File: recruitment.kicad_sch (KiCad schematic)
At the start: 18 parts

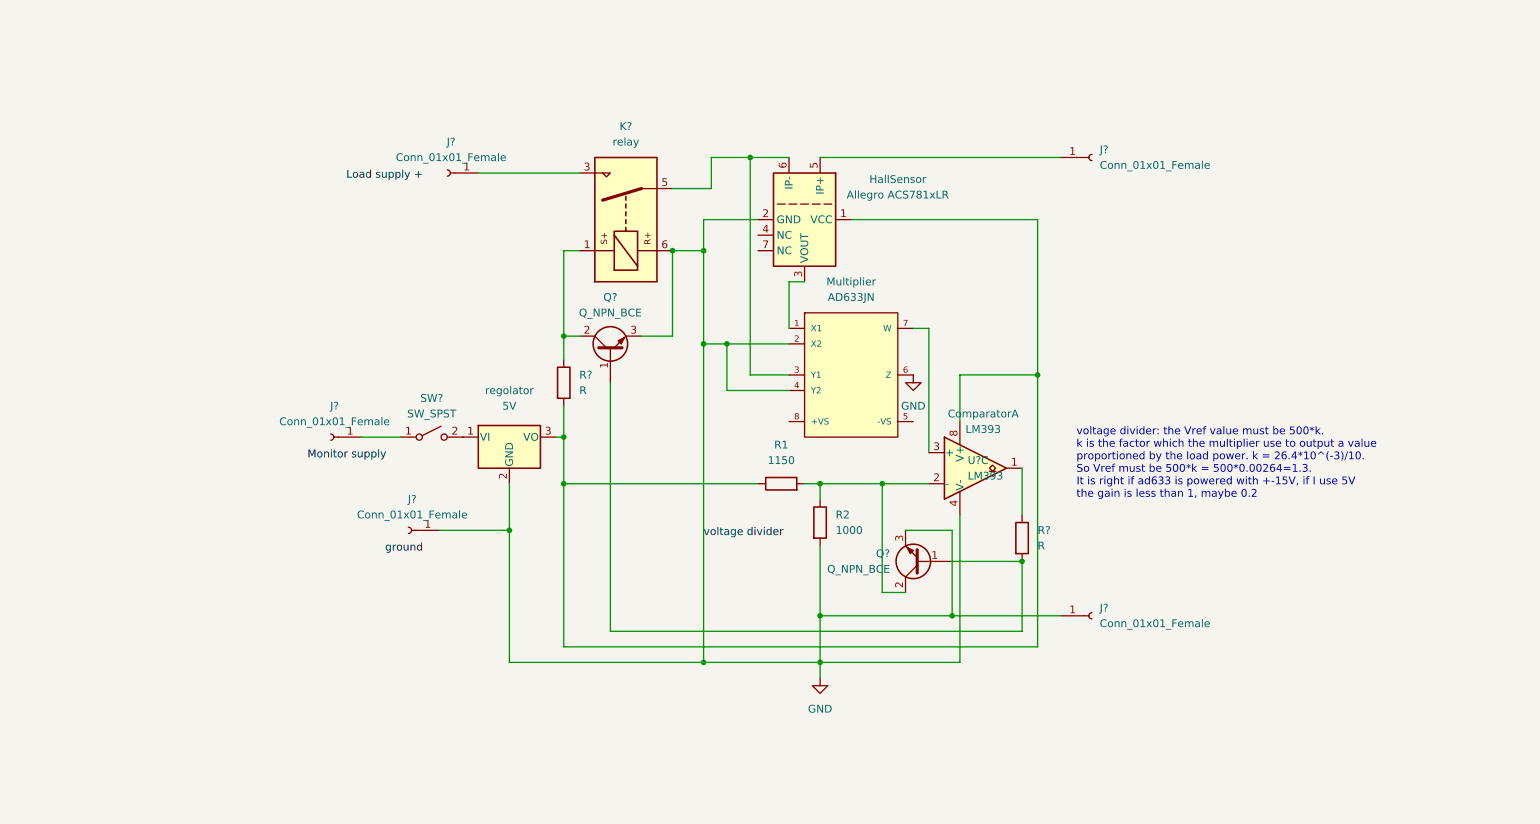
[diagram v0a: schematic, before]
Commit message: TODO: ad633 footprint
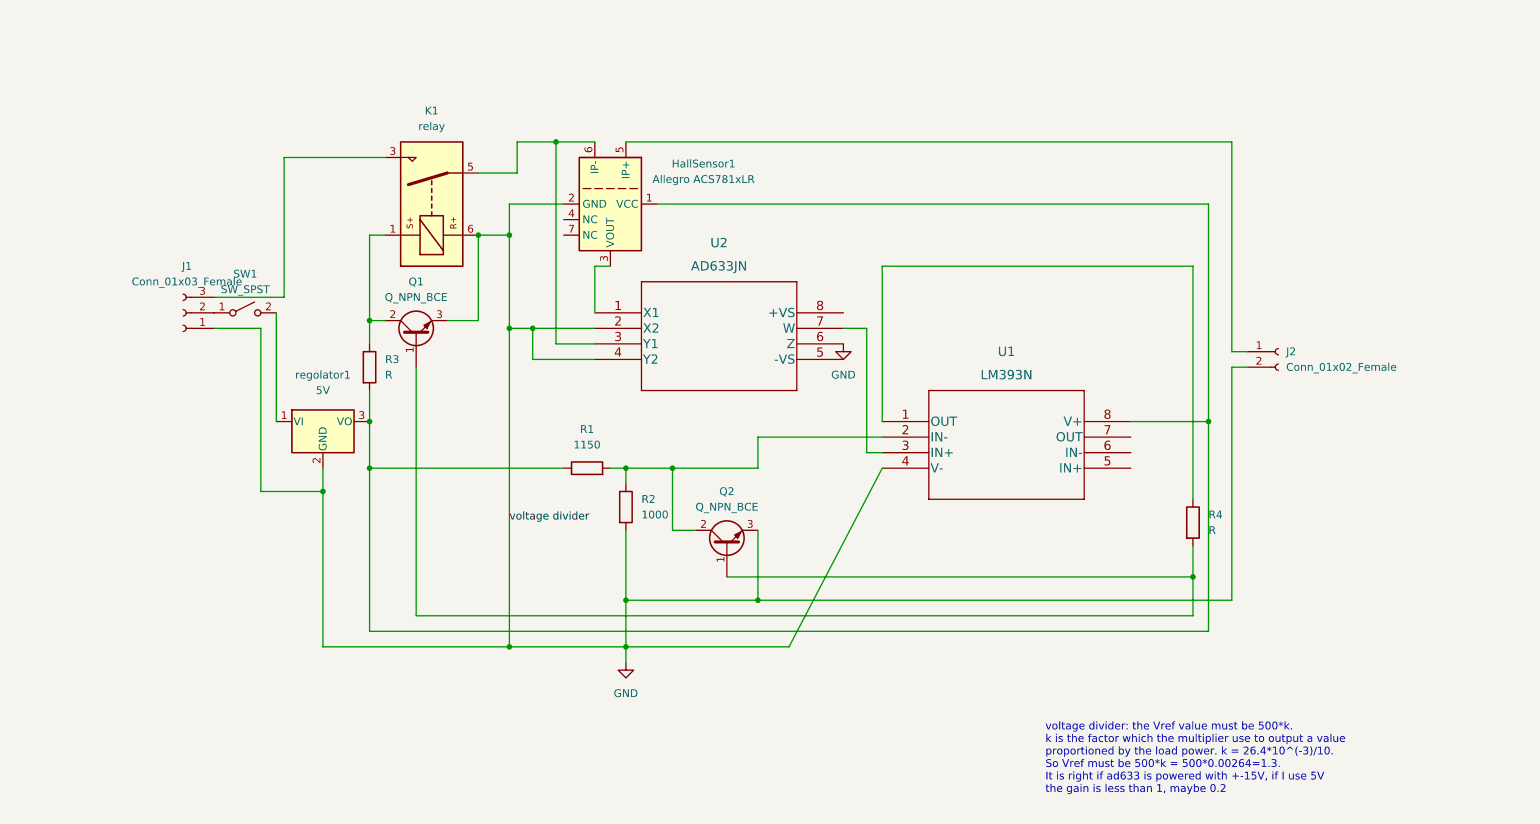
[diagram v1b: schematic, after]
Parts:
- removed Comparator, U?: LM393, symbol Comparator:LM393
- removed J? (x5): Conn_01x01_Female, symbol Connector:Conn_01x01_Female
- removed Multiplier: AD633JN, Analog_Devices-AD633JN-*, symbol eec:AD633JN
- added J1: Conn_01x03_Female, Connector_PinHeader_2.00mm:PinHeader_1x03_P2.00mm_Vertical, symbol Connector:Conn_01x03_Female
- added J2: Conn_01x02_Female, Connector_PinHeader_2.00mm:PinHeader_1x04_P2.00mm_Vertical, symbol Connector:Conn_01x02_Female
- added U1: LM393N, LM393:LM393N, symbol 2023-03-11_20-24-00:LM393N
- added U2: AD633JN, symbol 2023-03-11_21-32-38:AD633JN
- Q1, Q2: renamed from Q?; footprint (none) -> Package_TO_SOT_THT:TO-92_HandSolder
- R1, R2: footprint (none) -> Resistor_SMD:R_2816_7142Metric
- R3, R4: renamed from R?; footprint (none) -> Resistor_SMD:R_2816_7142Metric
- SW1: renamed from SW?; footprint (none) -> Button_Switch_SMD:SW_DIP_SPSTx01_Slide_6.7x4.1mm_W6.73mm_P2.54mm_LowProfile_JPin
- gave numbers to parts that had none: 1
- renumbered HallSensor to HallSensor1, regolator to regolator1
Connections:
- net GND: now also J1.1 (Pin_1), J2.2 (Pin_2), U1.4 (V-), U2.2 (X2), U2.4 (Y2), U2.6 (Z)
- net at Q2.2 (C), R1.2, R2.1: now also U1.2 (IN-)
- net at HallSensor1.1 (VCC), R1.1, R3.2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: now also U1.8 (V+)
- net at HallSensor1.3 (VOUT): now also U2.1 (X1)
- net at HallSensor1.5 (IP+): now also J2.1 (Pin_1)
- net at HallSensor1.6 (IP-), K1.5: now also U2.3 (Y1)
- net at R4.1: now also U1.1 (OUT)
- net at SW1.1 (A): now also J1.2 (Pin_2)
- net at K1.3: now also J1.3 (Pin_3)
- new net: U1.3 (IN+), U2.7 (W)
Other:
- moved on the sheet: HallSensor1, K1, Q1, Q2, R1, R2, R3, R4, SW1, regolator1

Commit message: footprints/autorouting done, TODO: understand transistor and optimize pcb shape
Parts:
- J2: footprint Connector_PinHeader_2.00mm:PinHeader_1x04_P2.00mm_Vertical -> Connector_PinHeader_2.00mm:PinHeader_1x02_P2.00mm_Vertical
- U2: footprint (none) -> LM393:LM393N
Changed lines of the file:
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@@
       (effects (font (size 1.524 1.524)))
     )
-    (property "Footprint" "" (id 2) (at 143.51 73.914 0)
+    (property "Footprint" "LM393:LM393N" (id 2) (at 143.51 73.914 0)
       (effects (font (size 1.524 1.524)) hide)
     )
@@
       (effects (font (size 1.27 1.27)) (justify left))
     )
-    (property "Footprint" "Connector_PinHeader_2.00mm:PinHeader_1x04_P2.00mm_Vertical" (id 2) (at 234.95 86.36 0)
+    (property "Footprint" "Connector_PinHeader_2.00mm:PinHeader_1x02_P2.00mm_Vertical" (id 2) (at 234.95 86.36 0)
       (effects (font (size 1.27 1.27)) hide)
     )
@@
     )
     (path "/9ef2c0bd-0176-4f0e-b213-c48663ceb734"
-      (reference "J2") (unit 1) (value "Conn_01x02_Female") (footprint "Connector_PinHeader_2.00mm:PinHeader_1x04_P2.00mm_Vertical")
+      (reference "J2") (unit 1) (value "Conn_01x02_Female") (footprint "Connector_PinHeader_2.00mm:PinHeader_1x02_P2.00mm_Vertical")
     )
     (path "/b4450c83-6da6-4393-a892-92bf8cbec8aa"
@@
     )
     (path "/02ec90e1-80ff-4a89-ad77-1717753cf5bc"
-      (reference "U2") (unit 1) (value "AD633JN") (footprint "")
+      (reference "U2") (unit 1) (value "AD633JN") (footprint "LM393:LM393N")
     )
     (path "/8bd72d47-aeb7-450d-acca-ccb14d6baac1"

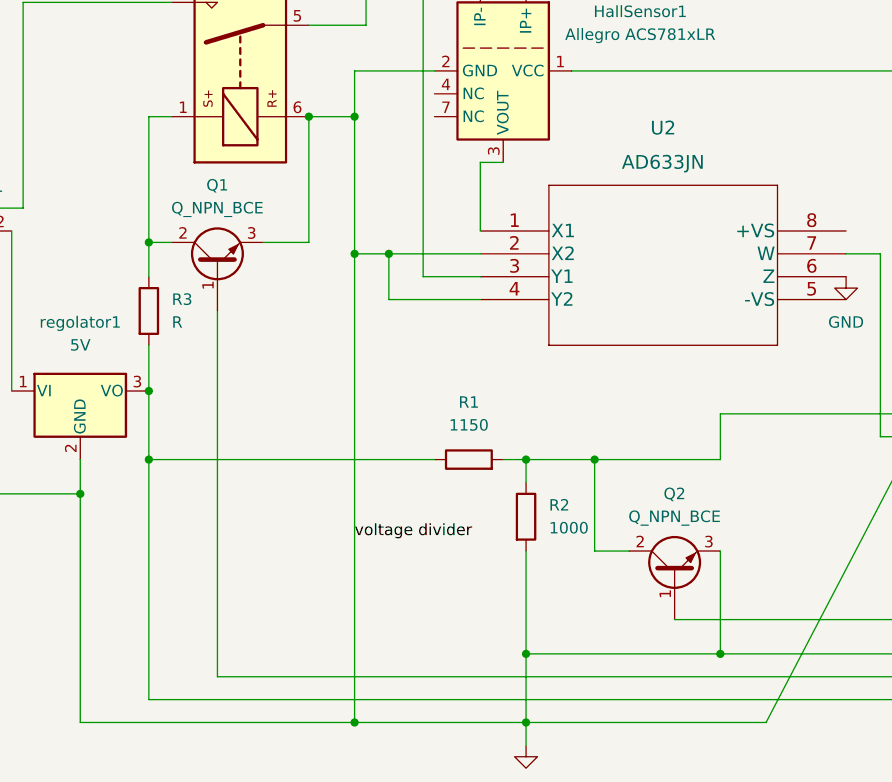
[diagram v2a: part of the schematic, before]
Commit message: better shape + MOSFET, TODO: adjust multiplier, it's better AD534
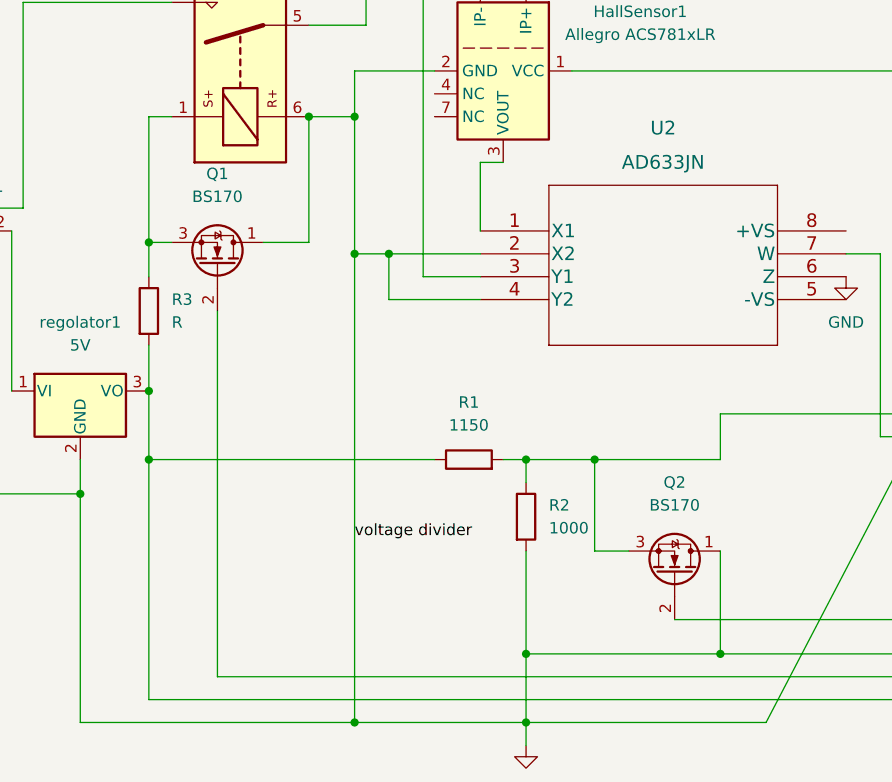
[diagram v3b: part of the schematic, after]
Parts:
- removed Q1, Q2: Q_NPN_BCE, Package_TO_SOT_THT:TO-92_HandSolder, symbol Device:Q_NPN_BCE
- added Q1, Q2: BS170, Package_TO_SOT_THT:TO-92_Inline, symbol Transistor_FET:BS170
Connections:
- net GND: now also Q1.1 (D), Q2.1 (D)
- net at R1.2, R2.1, U1.2 (IN-): now also Q2.3 (S)
- net at K1.1, R3.1: now also Q1.3 (S)
- net at R4.2: now also Q1.2 (G), Q2.2 (G)
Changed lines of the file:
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@@
     (pin "1")
+  )
+  (symbol (lib_id "Transistor_FET:BS170") (at 93.98 83.82 270) (mirror x) (unit 1)
+    (in_bom yes) (on_board yes) (fields_autoplaced)
+    (property "Reference" "Q1" (id 0) (at 93.98 73.66 90))
+    (property "Value" "BS170" (id 1) (at 93.98 76.2 90))
+    (property "Footprint" "Package_TO_SOT_THT:TO-92_Inline" (id 2) (at 92.075 78.74 0)
+      (effects (font (size 1.27 1.27) italic) (justify left) hide)
+    )
+    (property "Datasheet" "https://www.onsemi.com/pub/Collateral/BS170-D.PDF" (id 3) (at 93.98 83.82 0)
+      (effects (font (size 1.27 1.27)) (justify left) hide)
+    )
+    (pin "1")
+    (pin "2")
+    (pin "3")
   )
   (symbol (lib_id "Regulator_Linear:LM7805_TO220") (at 78.74 97.79 0) (unit 1)
@@
     (pin "8")
   )
-  (symbol (lib_id "Device:Q_NPN_BCE") (at 93.98 83.82 90) (unit 1)
+  (symbol (lib_id "Transistor_FET:BS170") (at 144.78 118.11 270) (mirror x) (unit 1)
     (in_bom yes) (on_board yes) (fields_autoplaced)
-    (property "Reference" "Q1" (id 0) (at 93.98 74.93 90))
-    (property "Value" "Q_NPN_BCE" (id 1) (at 93.98 77.47 90))
-    (property "Footprint" "Package_TO_SOT_THT:TO-92_HandSolder" (id 2) (at 91.44 78.74 0)
-      (effects (font (size 1.27 1.27)) hide)
+    (property "Reference" "Q2" (id 0) (at 144.78 107.95 90))
+    (property "Value" "BS170" (id 1) (at 144.78 110.49 90))
+    (property "Footprint" "Package_TO_SOT_THT:TO-92_Inline" (id 2) (at 142.875 113.03 0)
+      (effects (font (size 1.27 1.27) italic) (justify left) hide)
     )
-    (property "Datasheet" "~" (id 3) (at 93.98 83.82 0)
-      (effects (font (size 1.27 1.27)) hide)
-    )
-    (pin "1")
-    (pin "2")
-    (pin "3")
-  )
-  (symbol (lib_id "Device:Q_NPN_BCE") (at 144.78 118.11 90) (unit 1)
-    (in_bom yes) (on_board yes) (fields_autoplaced)
-    (property "Reference" "Q2" (id 0) (at 144.78 109.22 90))
-    (property "Value" "Q_NPN_BCE" (id 1) (at 144.78 111.76 90))
-    (property "Footprint" "Package_TO_SOT_THT:TO-92_HandSolder" (id 2) (at 142.24 113.03 0)
-      (effects (font (size 1.27 1.27)) hide)
-    )
-    (property "Datasheet" "~" (id 3) (at 144.78 118.11 0)
-      (effects (font (size 1.27 1.27)) hide)
+    (property "Datasheet" "https://www.onsemi.com/pub/Collateral/BS170-D.PDF" (id 3) (at 144.78 118.11 0)
+      (effects (font (size 1.27 1.27)) (justify left) hide)
     )
     (pin "1")
@@
       (reference "K1") (unit 1) (value "relay") (footprint "Relay_THT:Relay_1P1T_NO_10x24x18.8mm_Panasonic_ADW11xxxxW_THT")
     )
-    (path "/c28069b2-6ad3-4558-8513-38d165d26da9"
-      (reference "Q1") (unit 1) (value "Q_NPN_BCE") (footprint "Package_TO_SOT_THT:TO-92_HandSolder")
+    (path "/88d74566-2671-428d-917e-a1182c309ff5"
+      (reference "Q1") (unit 1) (value "BS170") (footprint "Package_TO_SOT_THT:TO-92_Inline")
     )
-    (path "/cd6e7e90-da37-4904-9164-3a30e73aa413"
-      (reference "Q2") (unit 1) (value "Q_NPN_BCE") (footprint "Package_TO_SOT_THT:TO-92_HandSolder")
+    (path "/f838928c-50f0-43ab-a7cb-907fcd79b114"
+      (reference "Q2") (unit 1) (value "BS170") (footprint "Package_TO_SOT_THT:TO-92_Inline")
     )
     (path "/424d5b31-88ca-4b43-8316-4aec53e16753"

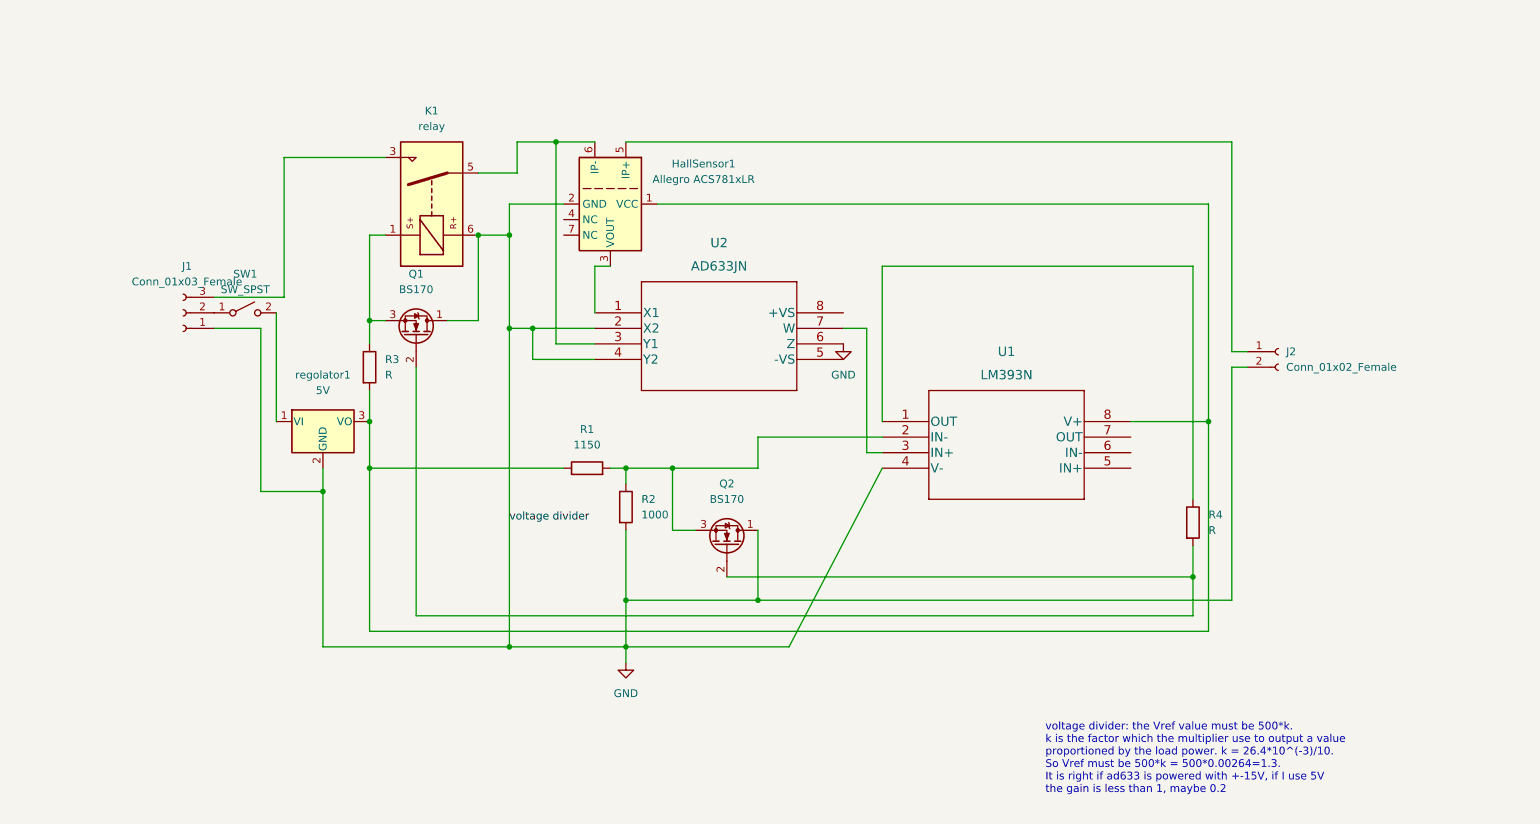
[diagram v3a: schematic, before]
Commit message: correct multiplier, TODO: check MOSFET
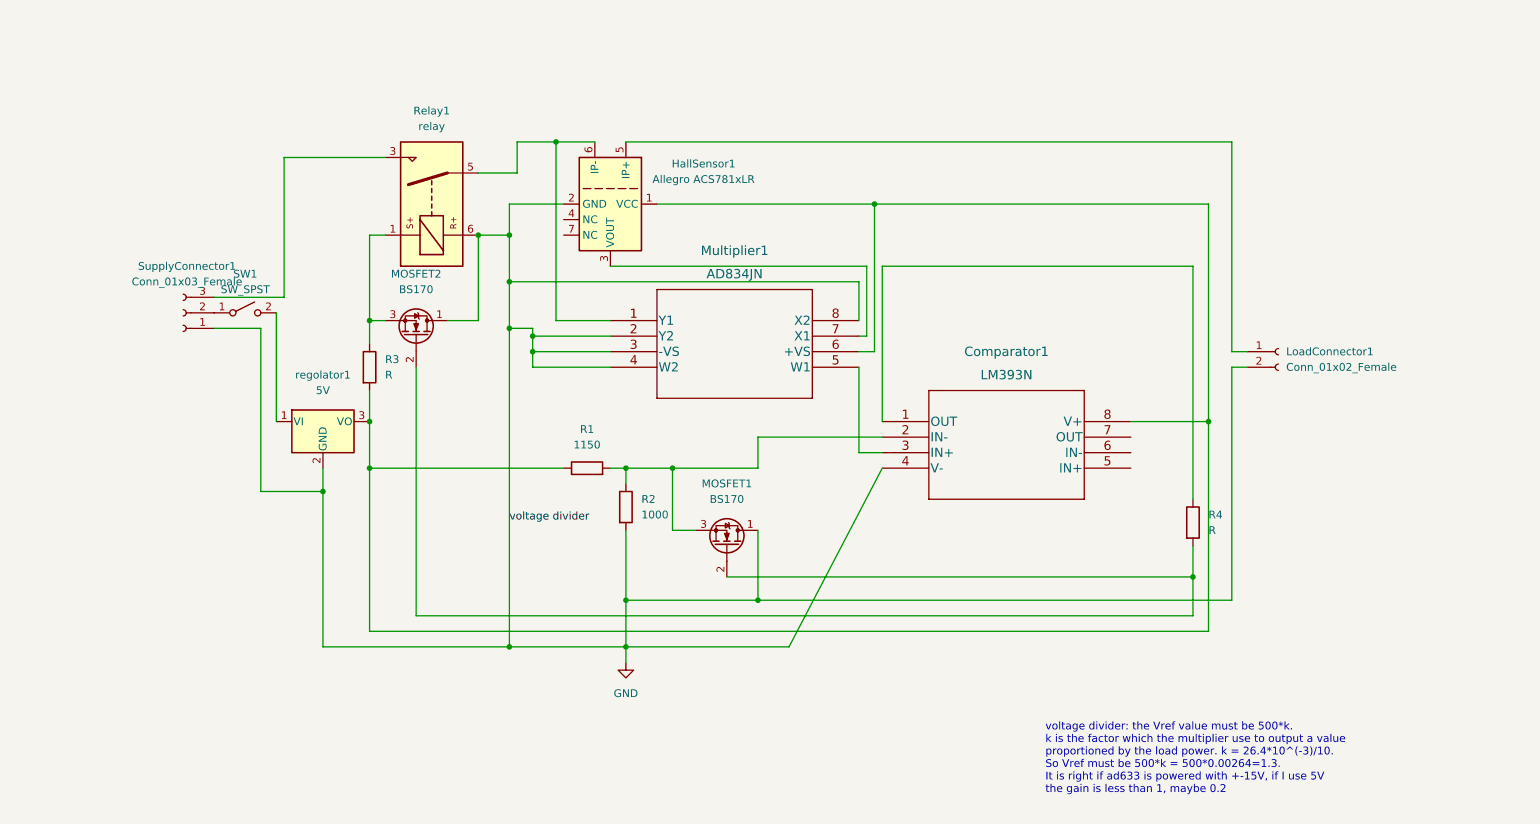
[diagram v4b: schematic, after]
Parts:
- removed U2: AD633JN, LM393:LM393N, symbol 2023-03-11_21-32-38:AD633JN
- added Multiplier1: AD834JN, LM393:LM393N, symbol 2023-03-13_17-57-03:AD834JN
- renumbered U1 to Comparator1, J2 to LoadConnector1, Q2 to MOSFET1, Q1 to MOSFET2, K1 to Relay1, J1 to SupplyConnector1
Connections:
- net GND: now also Multiplier1.2 (Y2), Multiplier1.3 (-VS), Multiplier1.4 (W2), Multiplier1.8 (X2)
- net at HallSensor1.3 (VOUT): now also Multiplier1.7 (X1)
- net at HallSensor1.6 (IP-), Relay1.5: now also Multiplier1.1 (Y1)
- net at Comparator1.3 (IN+): now also Multiplier1.5 (W1)
- net at Comparator1.8 (V+), HallSensor1.1 (VCC), R1.1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: now also Multiplier1.6 (+VS)
